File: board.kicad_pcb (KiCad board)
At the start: 6 copper layers, 197 x 139 mm, 34 parts, among them J2 Conn_2Rows-33Pins, J3 Conn_2Rows-33Pins, J4 Conn_2Rows-33Pins, J5 Conn_2Rows-33Pins, U1 MC68060RC50, U10 74LVC162245ADGG, U2 XC95144XL-5TQG100C, U3 SST39VF1601C-70-4C-EKE, U4 IS61WV51216BLL-10TLI, U5 IS61WV51216BLL-10TLI, U6 SST39VF1601C-70-4C-EKE, U7 74LVC162245ADGG, U8 74LVC162245ADGG, U9 74LVC162245ADGG

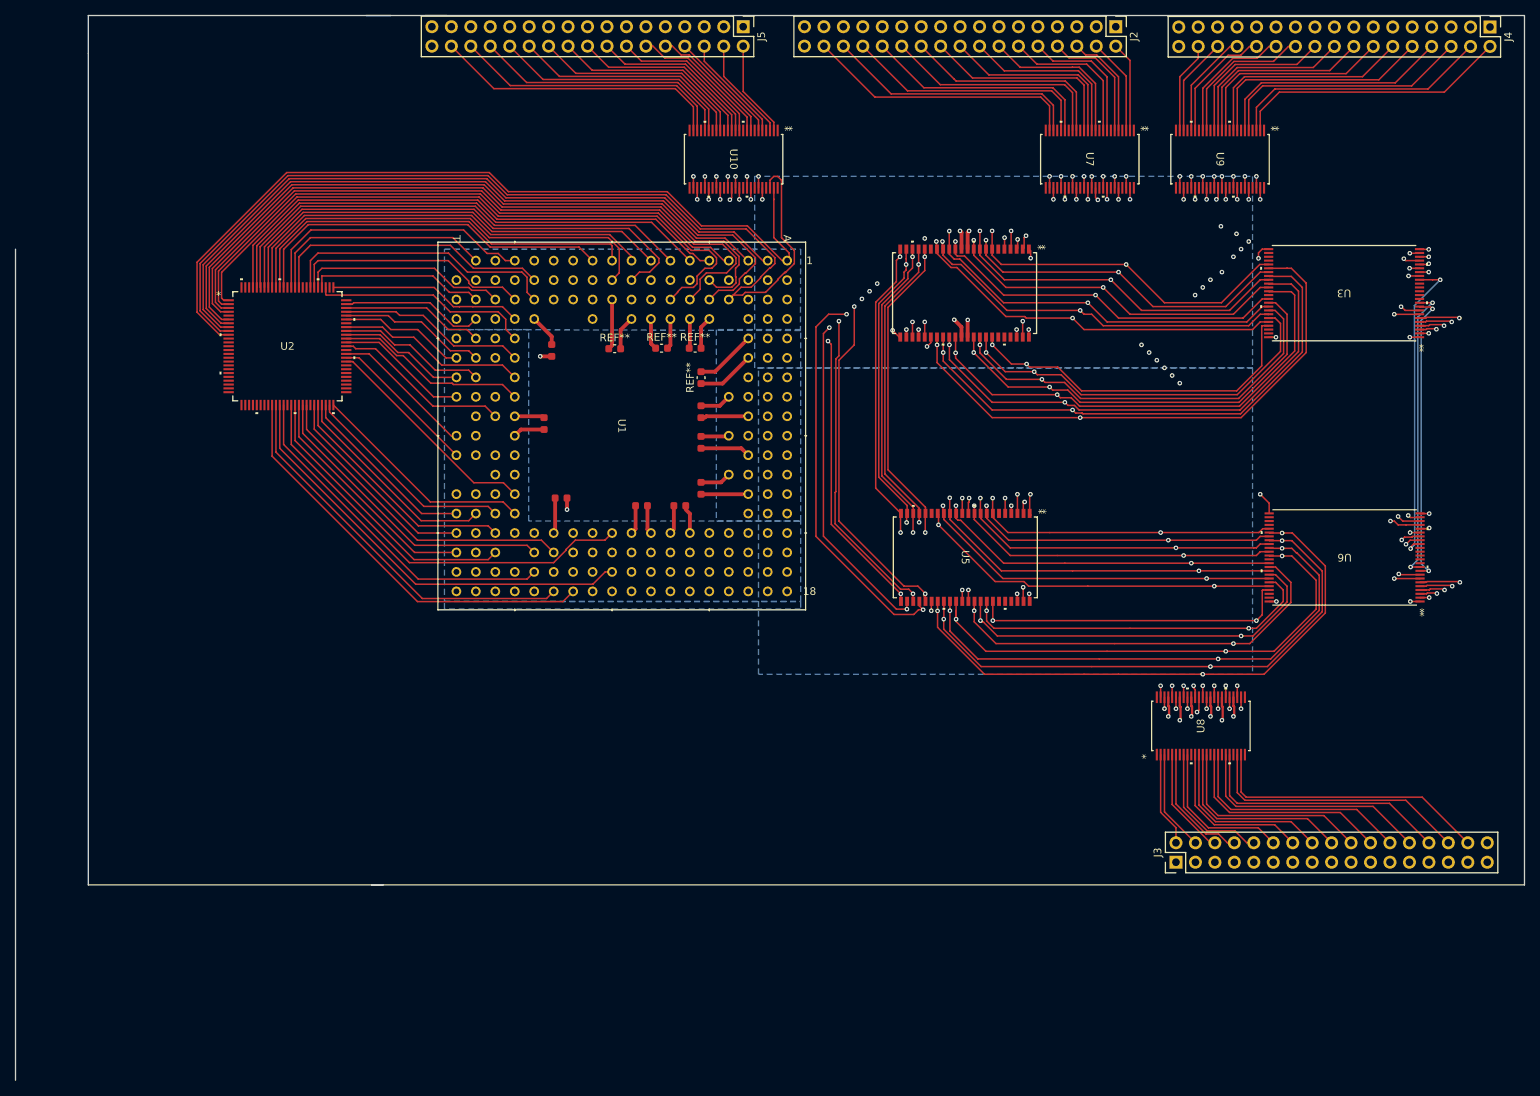
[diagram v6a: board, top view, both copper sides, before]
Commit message: Added ROM and RAM control signals
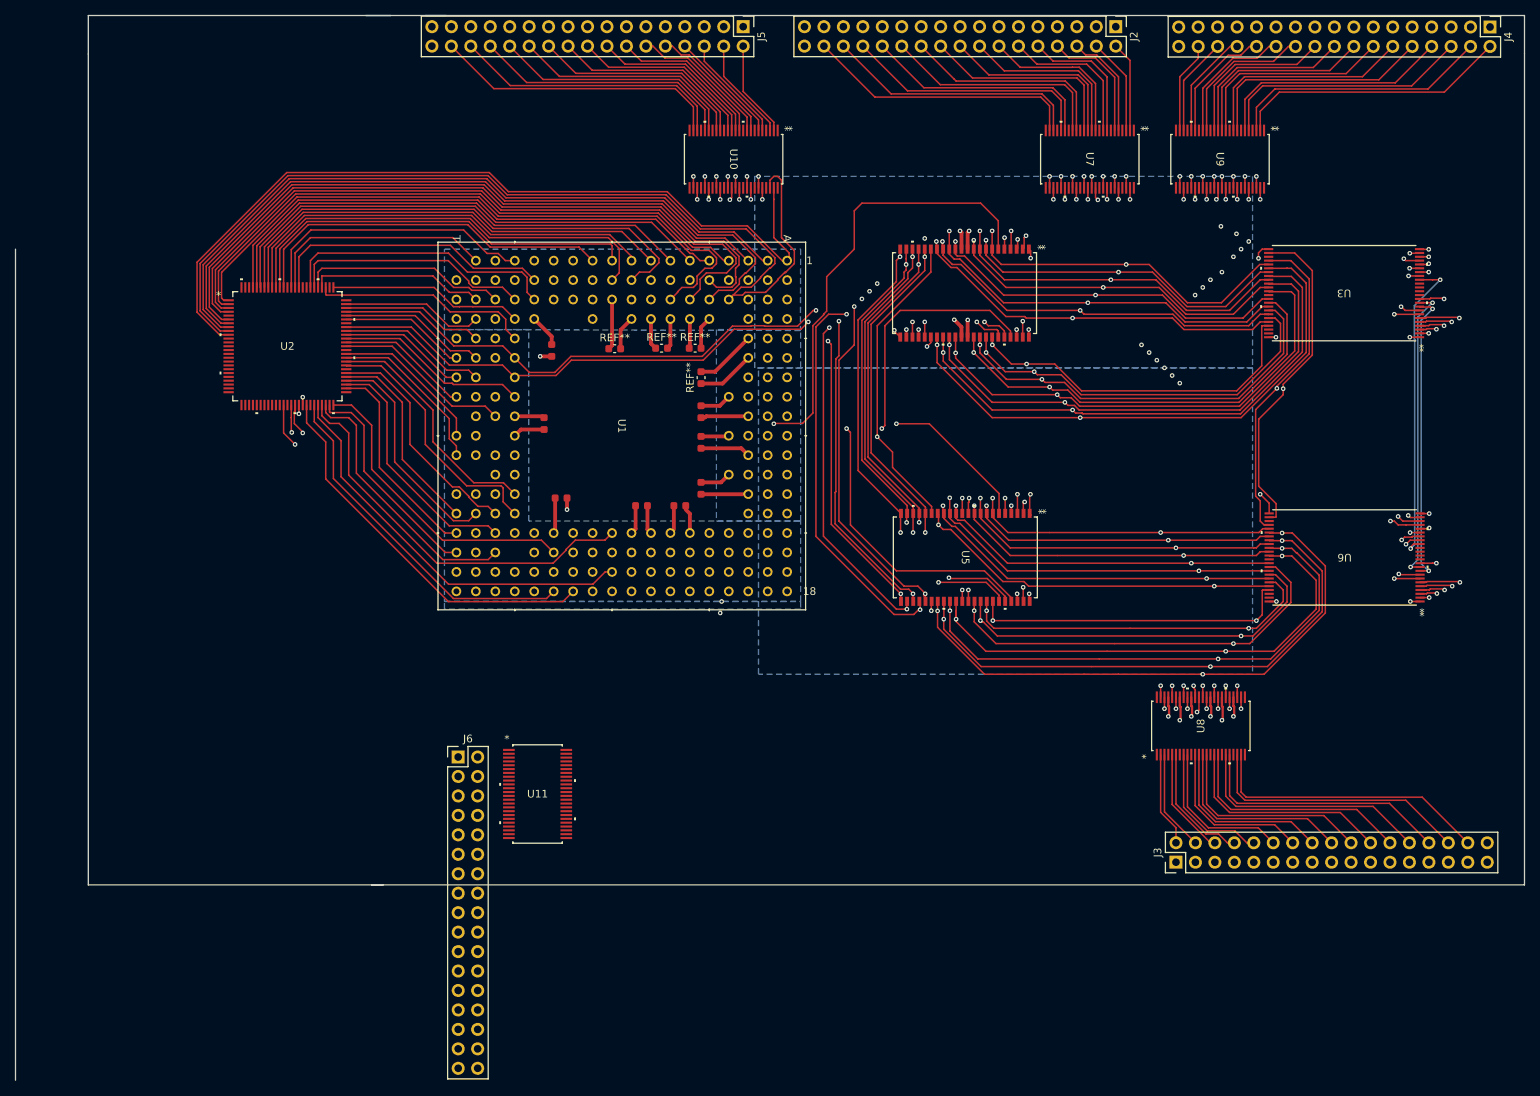
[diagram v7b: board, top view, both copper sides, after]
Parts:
- added J6: Conn_2Rows-33Pins, Connector_PinHeader_2.54mm:PinHeader_2x17_P2.54mm_Vertical, F.Cu at (66.3, 120.8)
- added U11: 74LVC162245ADGG, 74 buffer:SOT362-1_NEX, F.Cu at (76.7, 125.6)
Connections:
- U2 pad 34: /U1C-TM1 -> unconnected-(U2-IO-Pad34)
- U2 pad 35: /U1C-TM0 -> unconnected-(U2-IO-Pad35)
- U2 pad 36: /U1C-TM2 -> unconnected-(U2-IO-Pad36)
- U2 pad 37: /U1C-SIZ0 -> /RW
- U2 pad 39: /U1C-CLA -> /RAM_CS
- U2 pad 40: /U1C-TS -> /RAM_OE
- U2 pad 41: /U1C-PST3 -> /EPROM_CS
- U2 pad 42: /U1C-SIZ1 -> /EPROM_OE
- U2 pad 43: /U1C-RW -> /U1C-TM1
- U2 pad 45: /U1C-PST0 -> /U1C-TM0
- U2 pad 46: /U1C-TIP -> /U1C-TM2
- U2 pad 47: /U1C-PST1 -> /U1C-CLA
- U2 pad 48: /U1C-TA -> /U1C-TS
- U2 pad 49: /U1C-PST2 -> /U1C-PST3
- U2 pad 50: /U1C-SAS -> /U1C-RW
- U2 pad 52: unconnected-(U2-IO-Pad52) -> /U1C-PST0
- U2 pad 53: unconnected-(U2-IO-Pad53) -> /U1C-TIP
- U2 pad 54: unconnected-(U2-IO-Pad54) -> /U1C-PST1
- U2 pad 55: unconnected-(U2-IO-Pad55) -> /U1C-TA
- U2 pad 56: unconnected-(U2-IO-Pad56) -> /U1C-PST2
- U2 pad 58: unconnected-(U2-NC-Pad58) -> /U1C-SAS
- U3 pad 11: unconnected-(U3-*WE-Pad11) -> /RW
- U3 pad 26: unconnected-(U3-*CE-Pad26) -> /EPROM_CS
- U3 pad 27: unconnected-(U3-VSS-Pad27) -> /GND
- U3 pad 28: unconnected-(U3-*OE-Pad28) -> /EPROM_OE
- U3 pad 37: unconnected-(U3-VDD-Pad37) -> /VCC
- U3 pad 46: unconnected-(U3-VSS-Pad46) -> /GND
- U4 pad 11: unconnected-(U4-VDD-Pad11) -> /VCC
- U4 pad 12: unconnected-(U4-GND-Pad12) -> /GND
- U4 pad 17: unconnected-(U4-*WE-Pad17) -> /RW
- U4 pad 33: unconnected-(U4-VDD-Pad33) -> /VCC
- U4 pad 34: unconnected-(U4-GND-Pad34) -> /GND
- U4 pad 39: unconnected-(U4-*LB-Pad39) -> /BS3
- U4 pad 40: unconnected-(U4-*UB-Pad40) -> /BS2
- U4 pad 41: unconnected-(U4-*OE-Pad41) -> /RAM_OE
- U4 pad 6: unconnected-(U4-*CE-Pad6) -> /RAM_CS
- U5 pad 11: unconnected-(U5-VDD-Pad11) -> /VCC
- U5 pad 12: unconnected-(U5-GND-Pad12) -> /GND
- U5 pad 17: unconnected-(U5-*WE-Pad17) -> /RW
- U5 pad 33: unconnected-(U5-VDD-Pad33) -> /VCC
- U5 pad 34: unconnected-(U5-GND-Pad34) -> /GND
- U5 pad 39: unconnected-(U5-*LB-Pad39) -> /BS1
- U5 pad 40: unconnected-(U5-*UB-Pad40) -> /BS0
- U5 pad 41: unconnected-(U5-*OE-Pad41) -> /RAM_OE
- U5 pad 6: unconnected-(U5-*CE-Pad6) -> /RAM_CS
- U6 pad 11: unconnected-(U6-*WE-Pad11) -> /RW
- U6 pad 26: unconnected-(U6-*CE-Pad26) -> /EPROM_CS
- U6 pad 27: unconnected-(U6-VSS-Pad27) -> /GND
- U6 pad 28: unconnected-(U6-*OE-Pad28) -> /EPROM_OE
- U6 pad 37: /D27 -> /VCC
- U6 pad 46: unconnected-(U6-VSS-Pad46) -> /GND
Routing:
- net /RW: track 0.00 -> 238.6 mm, vias 0 -> 4
- net /EPROM_CS: track 0.00 -> 176.5 mm, vias 0 -> 2
- net /EPROM_OE: track 0.00 -> 173.8 mm, vias 0 -> 2
- net /RAM_CS: track 0.00 -> 161.0 mm, vias 0 -> 3
- net /RAM_OE: track 0.00 -> 150.9 mm, vias 0 -> 3
- net /BS0: track 25.4 -> 117.2 mm, vias 0 -> 2
- net /BS1: track 28.8 -> 118.0 mm, vias 0 -> 2
- net /BS2: track 24.5 -> 95.4 mm, vias 0 -> 2
- net /BS3: track 24.7 -> 93.8 mm, vias 0 -> 2
- net /U1C-SIZ0: track 45.5 -> 0.00 mm
- net /U1C-SIZ1: track 40.4 -> 0.00 mm
- net /VCC: track 58.8 -> 67.7 mm, vias 4 -> 6
- net /GND: track 66.2 -> 74.4 mm, vias 8 -> 10
- net /U1C-TM2: track 57.0 -> 52.5 mm
- net /U1C-TM0: track 50.7 -> 46.3 mm
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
